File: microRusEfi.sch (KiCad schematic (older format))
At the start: 14 parts, among them U3 Molex_48_pin

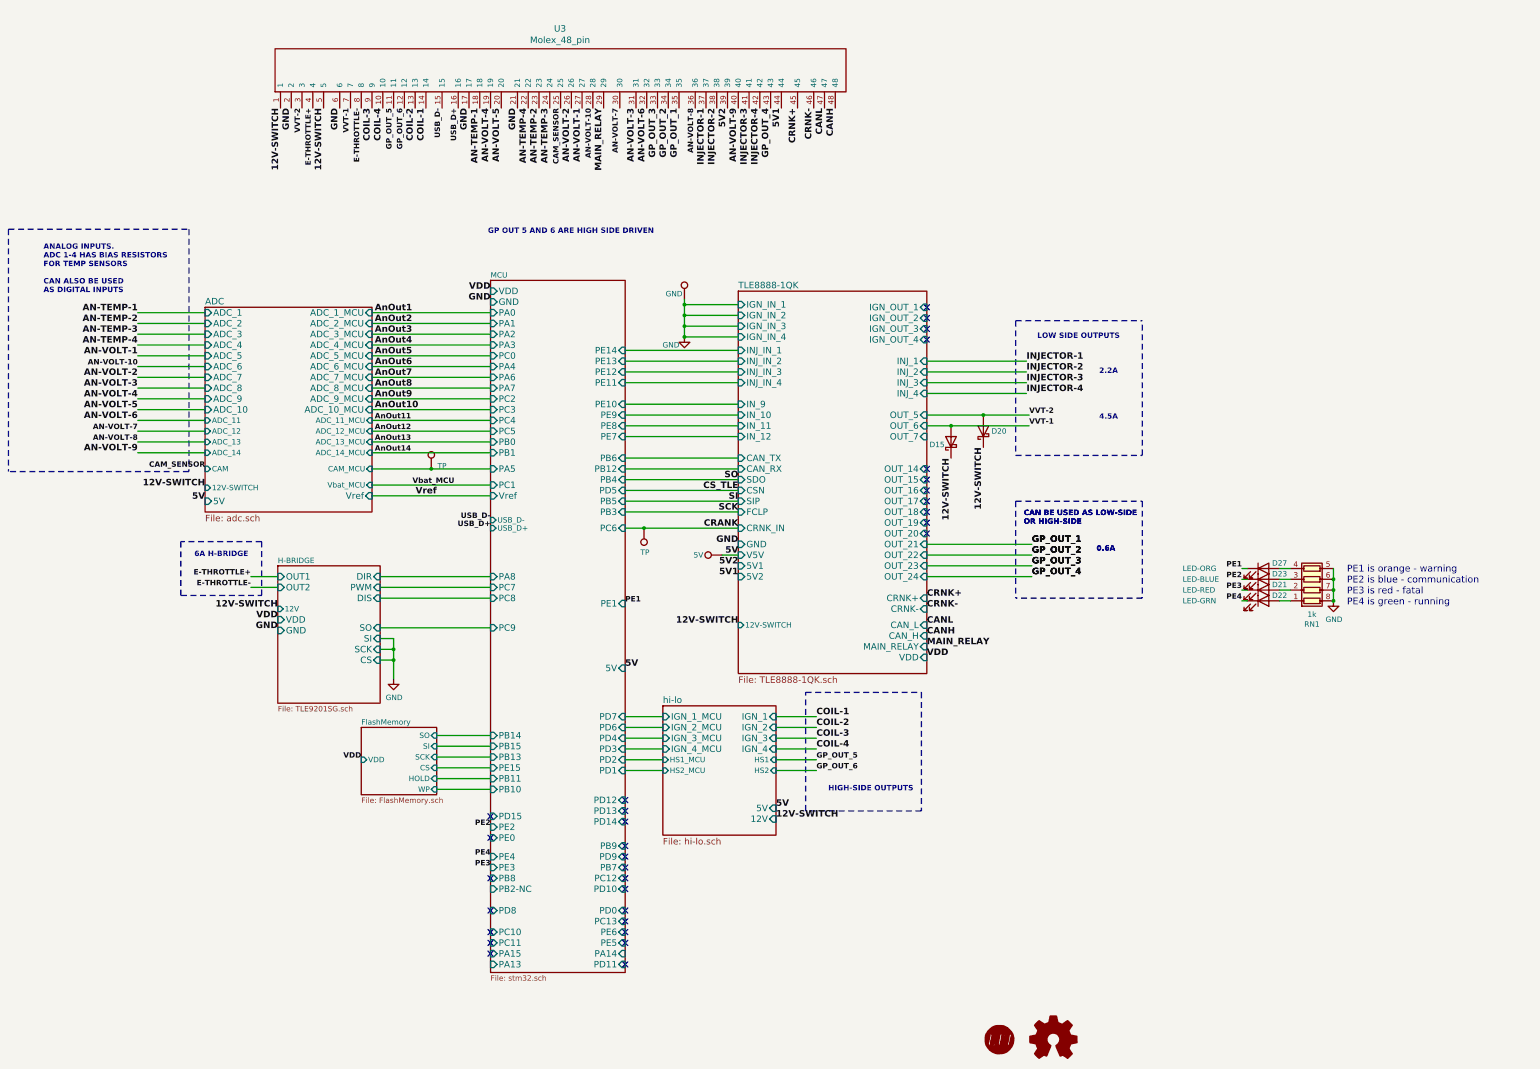
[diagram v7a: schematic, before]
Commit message: Some unused pads exposed to be accessible as test points, etc.
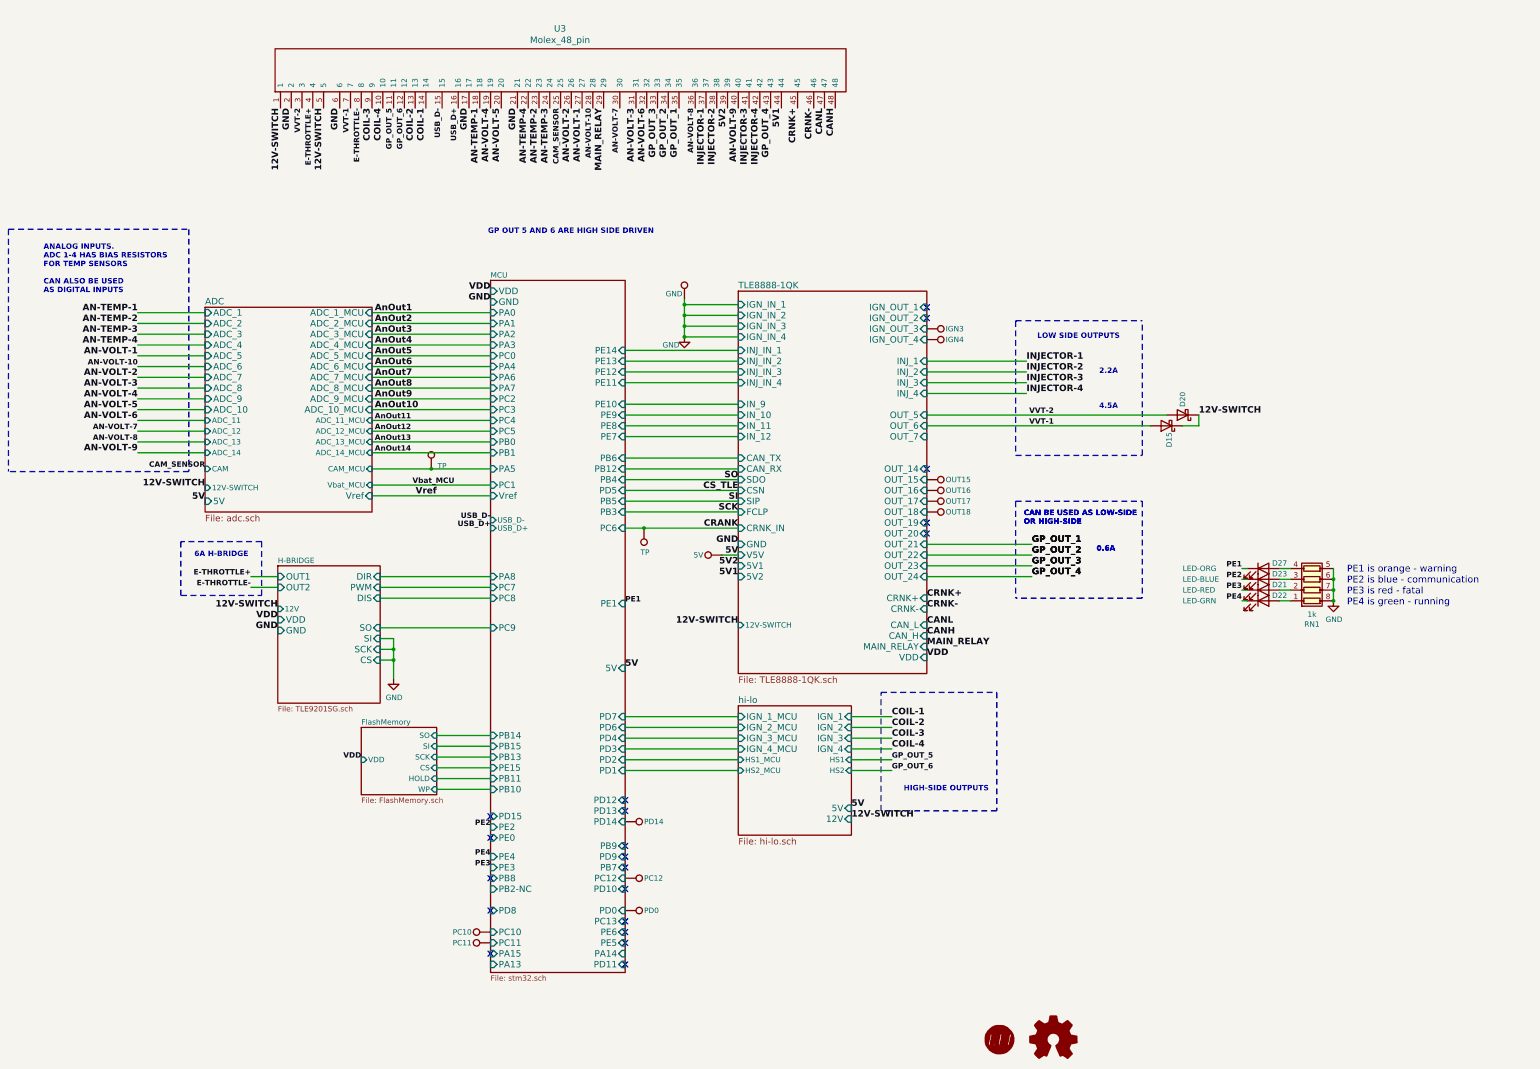
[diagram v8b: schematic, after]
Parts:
- added IGN3: IGN3, Connector_Pin:Pin_D0.7mm_L6.5mm_W1.8mm_FlatFork, symbol Connector:TestPoint
- added IGN4: IGN4, Connector_Pin:Pin_D0.7mm_L6.5mm_W1.8mm_FlatFork, symbol Connector:TestPoint
- added OUT15: OUT15, Connector_Pin:Pin_D0.7mm_L6.5mm_W1.8mm_FlatFork, symbol Connector:TestPoint
- added OUT16: OUT16, Connector_Pin:Pin_D0.7mm_L6.5mm_W1.8mm_FlatFork, symbol Connector:TestPoint
- added OUT17: OUT17, Connector_Pin:Pin_D0.7mm_L6.5mm_W1.8mm_FlatFork, symbol Connector:TestPoint
- added OUT18: OUT18, Connector_Pin:Pin_D0.7mm_L6.5mm_W1.8mm_FlatFork, symbol Connector:TestPoint
- added PC10: PC10, Connector_Pin:Pin_D0.7mm_L6.5mm_W1.8mm_FlatFork, symbol Connector:TestPoint
- added PC11: PC11, Connector_Pin:Pin_D0.7mm_L6.5mm_W1.8mm_FlatFork, symbol Connector:TestPoint
- added PC12: PC12, Connector_Pin:Pin_D0.7mm_L6.5mm_W1.8mm_FlatFork, symbol Connector:TestPoint
- added PD0: PD0, Connector_Pin:Pin_D0.7mm_L6.5mm_W1.8mm_FlatFork, symbol Connector:TestPoint
- added PD14: PD14, Connector_Pin:Pin_D0.7mm_L6.5mm_W1.8mm_FlatFork, symbol Connector:TestPoint
- LOGO1: footprint modules:Logo -> rusEFI:LogoMRE
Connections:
- net MCU/PC10: now also PC10.1
- net MCU/PC11: now also PC11.1
- net MCU/PC12: now also PC12.1
- net MCU/PD0: now also PD0.1
- net MCU/PD14: now also PD14.1
- net TLE8888-1QK/IGN_OUT_3: now also IGN3.1
- net TLE8888-1QK/IGN_OUT_4: now also IGN4.1
- net TLE8888-1QK/OUT_15: now also OUT15.1
- net TLE8888-1QK/OUT_16: now also OUT16.1
- net TLE8888-1QK/OUT_17: now also OUT17.1
- net TLE8888-1QK/OUT_18: now also OUT18.1
- no-connect marks 31 -> 20
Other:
- moved on the sheet: D15, D20
